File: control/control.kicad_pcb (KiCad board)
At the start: 2 copper layers, 140 x 103.2 mm, 137 parts, among them IC1 TJA1040, IC2 DNP MAX481CSA, IC3 ST232BD, IC4 ATMEGA128-A, IC5 ST232BD, IC6 FT232RL, J4 POWER, P1 SENSOR, P10 DB9, P11 USB_B, P12 USB_OTG, P13 DB9, P2 I2C0, P3 I2C1, P4 I2C2, P5 COIN, P6 CONN_02X13, P7 ISP, P8 12V, P9 5V, U1 DNP LM2940-N 5V, X1 16MHz

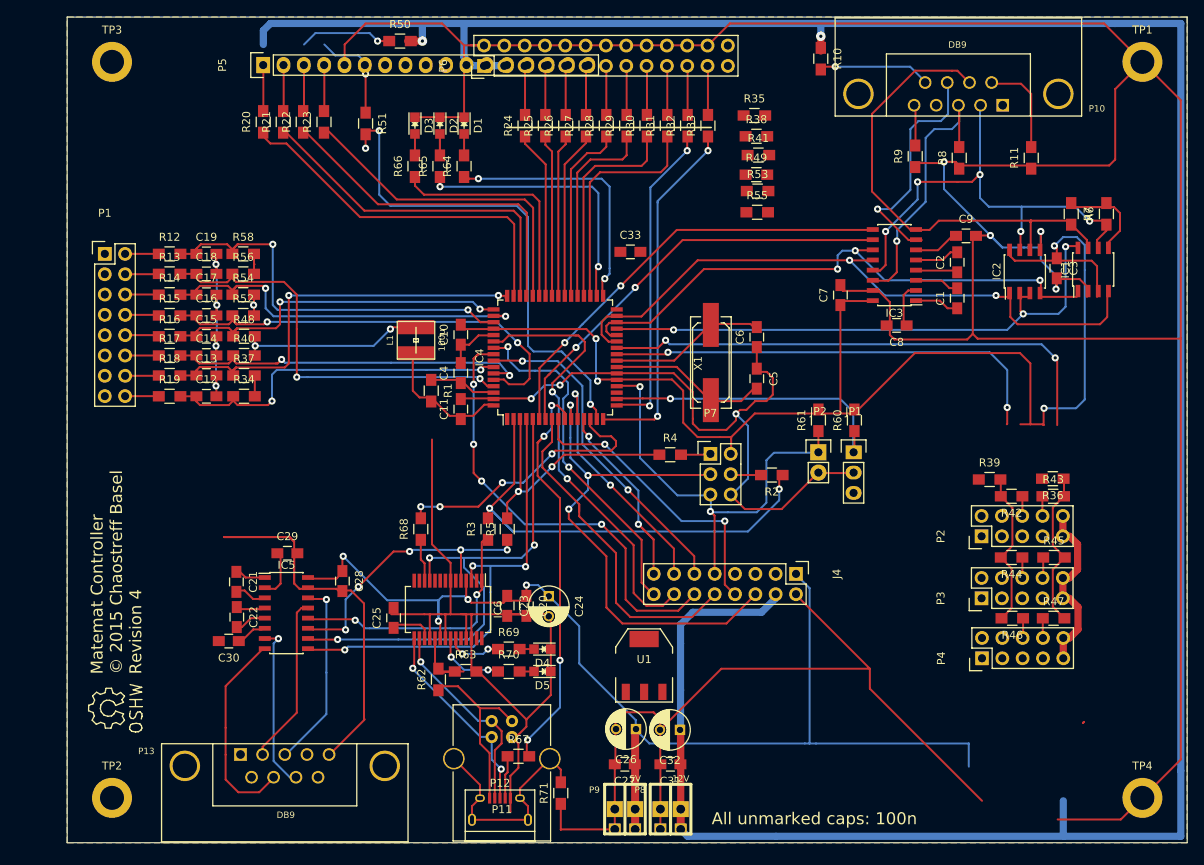
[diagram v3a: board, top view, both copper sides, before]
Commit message: WIP control board rewiring to make it smaller
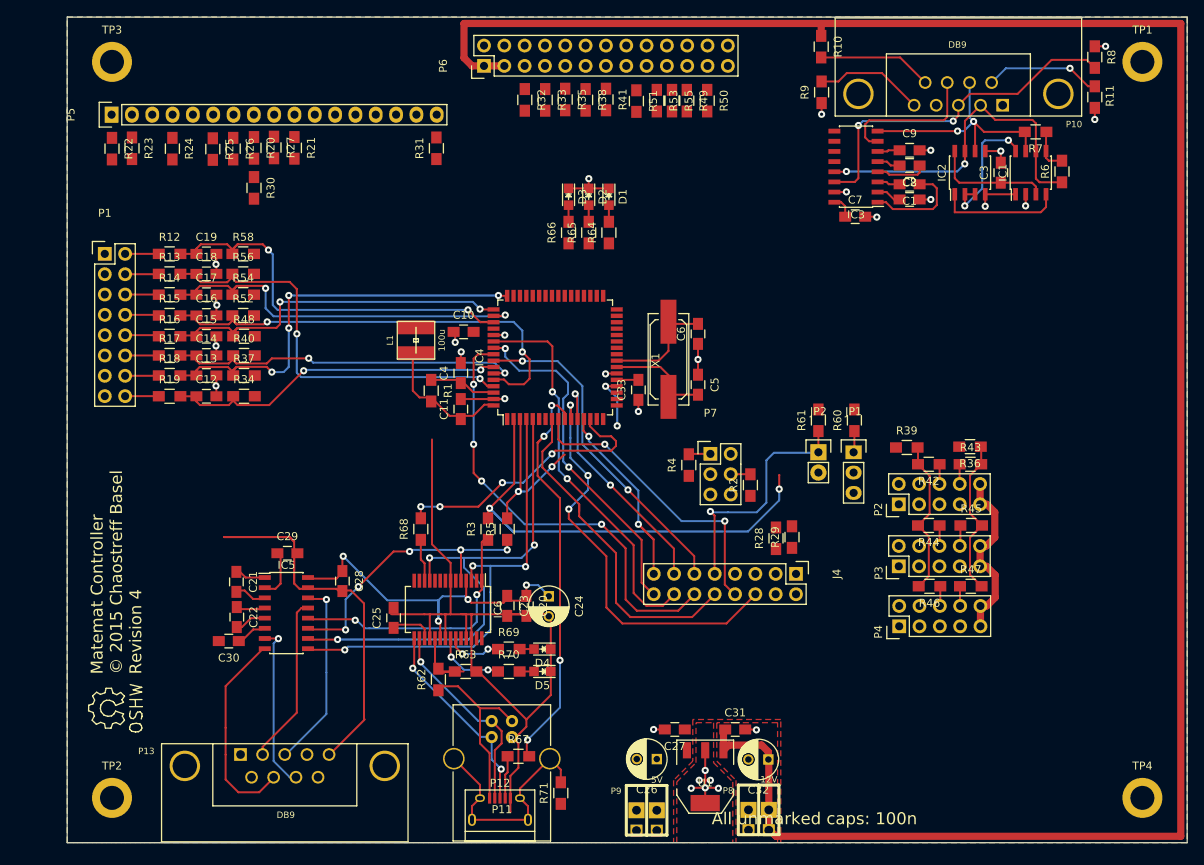
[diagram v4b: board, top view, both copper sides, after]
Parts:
- C26: value 10u -> 22u
- moved R28 55.8 mm to (138.6, 122.0)
- moved R29 55.4 mm to (140.6, 121.8)
- moved R30 49.7 mm to (73.3, 78.2), turned to 270 degrees
- moved R24 44.2 mm to (63.1, 73.2), turned to 270 degrees
- moved R25 41.7 mm to (68.2, 73.3), turned to 270 degrees
- moved R26 41.7 mm to (70.8, 73.2), turned to 270 degrees
- moved R50 39.1 mm to (130.0, 67.2), turned to 270 degrees
- moved R27 39.1 mm to (75.8, 73.1), turned to 270 degrees
- moved R51 34.0 mm to (121.2, 67.3)
- moved R31 29.0 mm to (96.2, 73.2)
- moved R23 24.2 mm to (58.1, 73.2), turned to 270 degrees
- moved R22 24.1 mm to (55.6, 73.2), turned to 270 degrees
- moved R35 23.7 mm to (112.2, 67.1), turned to 270 degrees
- moved R38 21.8 mm to (114.8, 67.2), turned to 270 degrees
- moved D3 21.2 mm to (112.7, 79.3)
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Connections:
- IC4 pad 30: (no net) -> /UART1_RTS
- IC4 pad 31: (no net) -> /UART1_CTS
- IC4 pad 6: /UART1_RTS -> (no net)
- IC4 pad 7: /UART1_CTS -> (no net)
- R34 pad 2: Net-(R34-Pad2) -> VCC
- R37 pad 2: Net-(R34-Pad2) -> VCC
- R40 pad 2: Net-(R34-Pad2) -> VCC
- R48 pad 2: Net-(R34-Pad2) -> VCC
- R52 pad 2: Net-(R34-Pad2) -> VCC
- R54 pad 2: Net-(R34-Pad2) -> VCC
- R56 pad 2: Net-(R34-Pad2) -> VCC
- R58 pad 2: Net-(R34-Pad2) -> VCC
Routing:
- net GND: track 785.0 -> 221.8 mm, vias 11 -> 29
- net VCC: track 450.4 -> 68.4 mm, vias 12 -> 4
- net +12V: track 368.3 -> 295.8 mm, vias 2 -> 0
- net /SDA: track 91.7 -> 19.9 mm, vias 2 -> 0
- net /SCL: track 86.1 -> 19.7 mm, vias 2 -> 0
- net /UART1_TX: track 71.5 -> 5.29 mm, vias 3 -> 1
- net /UART1_RX: track 80.7 -> 15.5 mm, vias 2 -> 0
- net /COIN_OUT_A: track 63.0 -> 0.00 mm
- net /BILL_OUT_FULL: track 61.6 -> 0.00 mm, vias 3 -> 0
- net /UART1_RTS: track 55.1 -> 0.00 mm, vias 2 -> 0
- net /UART1_CTS: track 53.2 -> 0.00 mm, vias 2 -> 0
- net /CAN_SLEEP: track 69.7 -> 16.6 mm, vias 3 -> 2
- net /BILL_OUT_VALID: track 37.8 -> 0.00 mm, vias 1 -> 0
- net /~FLASH_EN~: track 38.7 -> 3.33 mm, vias 1 -> 0
- net /LED B: track 34.6 -> 0.00 mm, vias 2 -> 0
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- added copper zone on F.Cu, net +12V
- added copper zone on F.Cu, net GND

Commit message: Update and cleanup for KiCAD 5
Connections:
- IC4 pad 1: (no net) -> Net-(IC4-Pad1)
- IC4 pad 19: (no net) -> Net-(IC4-Pad19)
- IC4 pad 6: (no net) -> Net-(IC4-Pad6)
- IC4 pad 7: (no net) -> Net-(IC4-Pad7)
- IC6 pad 10: (no net) -> Net-(IC6-Pad10)
- IC6 pad 13: (no net) -> Net-(IC6-Pad13)
- IC6 pad 14: (no net) -> Net-(IC6-Pad14)
- IC6 pad 2: (no net) -> Net-(IC6-Pad2)
- IC6 pad 27: (no net) -> Net-(IC6-Pad27)
- IC6 pad 28: (no net) -> Net-(IC6-Pad28)
- IC6 pad 6: (no net) -> Net-(IC6-Pad6)
- IC6 pad 9: (no net) -> Net-(IC6-Pad9)
- J4 pad 3: (no net) -> Net-(J4-Pad3)
- JP1 pad 3: (no net) -> Net-(JP1-Pad3)
- P10 pad 1: (no net) -> Net-(P10-Pad1)
- P10 pad 4: (no net) -> Net-(P10-Pad4)
- P13 pad 1: (no net) -> Net-(P13-Pad1)
- P13 pad 4: (no net) -> Net-(P13-Pad4)
- P13 pad 6: (no net) -> Net-(P13-Pad6)
- P13 pad 9: (no net) -> Net-(P13-Pad9)
- P5 pad 5: (no net) -> Net-(P5-Pad5)
- P6 pad 25: (no net) -> Net-(P6-Pad25)
- R67 pad 2: (no net) -> /USBID

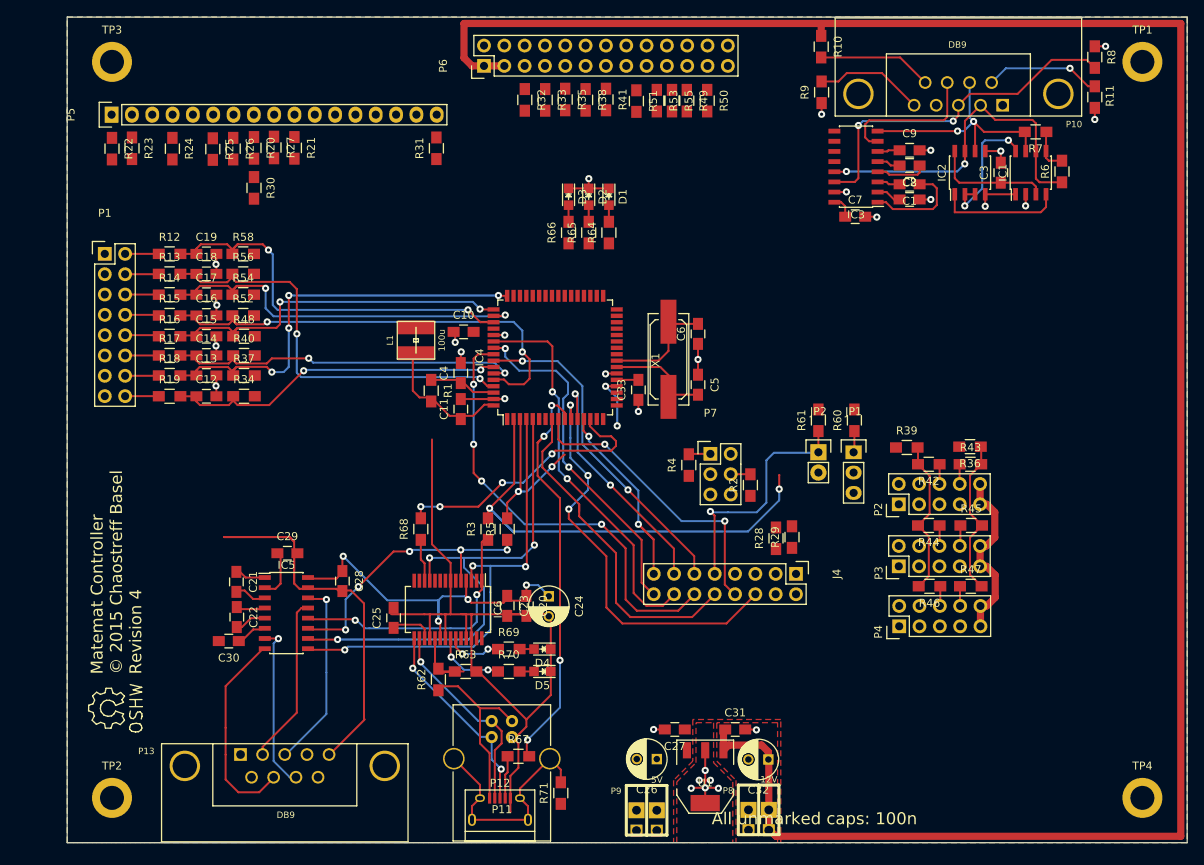
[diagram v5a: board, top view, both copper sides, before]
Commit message: Made board smaller and started rerouting
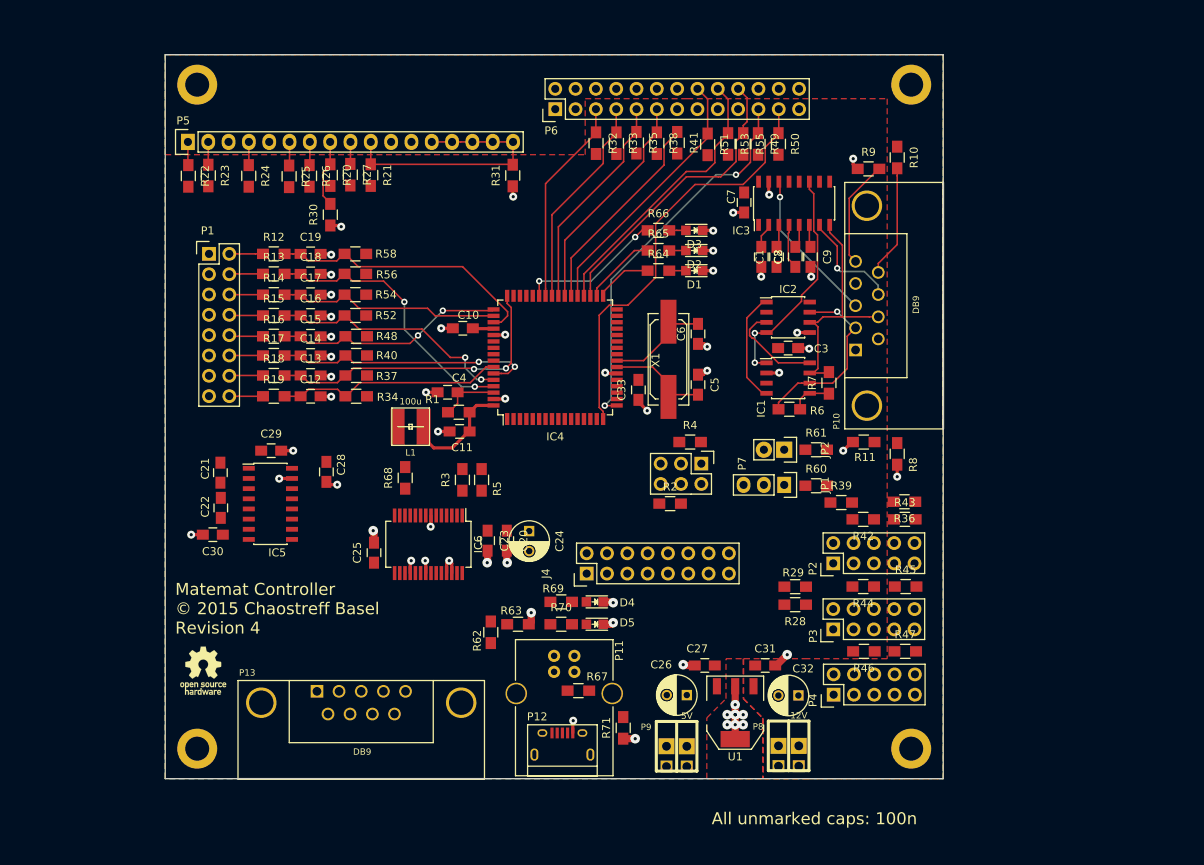
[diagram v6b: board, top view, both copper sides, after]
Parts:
- removed ?: Symbol_OSHW-Logo_SilkScreen, Symbols:Symbol_OSHW-Logo_SilkScreen
- added REF**: OSHW-Logo_5.7x6mm_SilkScreen, Symbol:OSHW-Logo_5.7x6mm_SilkScreen, F.Cu at (67.0, 138.5)
- moved R8 55.4 mm to (153.8, 111.4), turned to 90 degrees
- moved R11 51.9 mm to (149.6, 109.9), turned to 0 degrees
- moved R6 45.2 mm to (140.3, 105.8), turned to 0 degrees
- moved R7 40.6 mm to (145.2, 102.5), turned to 90 degrees
- moved IC1 39.7 mm to (140.1, 101.9), turned to 0 degrees
- moved C3 34.5 mm to (140.1, 98.2), turned to 0 degrees
- moved TP4 29.5 mm to (155.5, 148.2)
- moved IC2 29.0 mm to (140.1, 94.3), turned to 0 degrees
- moved TP1 29.0 mm to (155.5, 65.2)
- moved P10 28.8 mm to (150.0, 92.9), turned to 270 degrees
- moved J4 26.2 mm to (114.9, 126.4), turned to 90 degrees
- moved C8 19.9 mm to (136.8, 86.8), turned to 270 degrees
- moved C1 18.9 mm to (138.7, 86.8), turned to 90 degrees
- moved C2 18.3 mm to (141.0, 86.8), turned to 90 degrees
- moved C9 18.2 mm to (142.9, 86.8), turned to 270 degrees
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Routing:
- net +12V: track 295.8 -> 0.00 mm
- net GND: track 221.8 -> 85.7 mm, vias 29 -> 58
- net VCC: track 68.4 -> 2.61 mm, vias 4 -> 0
- net /UART0_CTS: track 64.1 -> 0.00 mm, vias 3 -> 0
- net Net-(IC4-Pad2): track 60.5 -> 0.00 mm, vias 2 -> 0
- net /UART0_RTS: track 58.2 -> 0.00 mm, vias 3 -> 0
- net /JTAG TMS: track 56.2 -> 0.00 mm, vias 4 -> 0
- net /BILL_OUT_FULL: track 0.00 -> 53.1 mm
- net /SCK: track 52.0 -> 0.00 mm, vias 3 -> 0
- net /JTAG TDI: track 48.9 -> 0.00 mm, vias 2 -> 0
- net /BILL_OUT_VALID: track 0.00 -> 48.2 mm, vias 0 -> 2
- net /JTAG TDO: track 43.2 -> 0.00 mm, vias 2 -> 0
- net /strobe: track 42.3 -> 0.00 mm
- net /JTAG TCK: track 41.8 -> 0.00 mm, vias 2 -> 0
- net /~RST~: track 39.3 -> 0.00 mm, vias 3 -> 0
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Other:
- board size 140 x 103.2 mm -> 97.2 x 90.5 mm
- net class Default: trace_width 0.25 -> 0.2; via_dia 0.9 -> 0.8
- net class Power: trace_width 0.9 -> 0.4; via_dia 1.2 -> 1
- rule via_min_size: 0.9 -> 0.8

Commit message: More rerouting
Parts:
- moved J4 15.4 mm to (130.0, 129.4), turned to 180 degrees
- moved R2 11.3 mm to (117.1, 125.4)
- moved R4 11.3 mm to (119.6, 117.7)
- moved P7 11.3 mm to (121.0, 120.4)
- moved R36 2.31 mm to (152.3, 117.5)
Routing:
- net /UART0_RTS: track 0.00 -> 45.8 mm
- net /UART0_CTS: track 0.00 -> 45.1 mm, vias 0 -> 2
- net /SDA: track 0.00 -> 38.6 mm, vias 0 -> 2
- net /~RST~: track 0.00 -> 36.3 mm
- net Net-(IC5-Pad14): track 0.00 -> 34.7 mm
- net Net-(IC6-Pad16): track 0.00 -> 34.2 mm
- net Net-(IC6-Pad15): track 0.00 -> 33.7 mm, vias 0 -> 1
- net Net-(IC5-Pad7): track 0.00 -> 33.7 mm
- net Net-(IC5-Pad8): track 0.00 -> 31.4 mm
- net /UART0_TX: track 0.00 -> 31.0 mm, vias 0 -> 3
- net Net-(IC4-Pad2): track 0.00 -> 29.8 mm, vias 0 -> 2
- net /SCK: track 0.00 -> 29.6 mm
- net Net-(IC5-Pad13): track 0.00 -> 28.2 mm
- net /SCL: track 0.00 -> 26.1 mm
- net /UART0_RX: track 0.00 -> 25.4 mm, vias 0 -> 2
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- added copper zone on F.Cu, net Net-(P11-Pad5)
